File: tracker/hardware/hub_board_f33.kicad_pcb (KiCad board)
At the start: 2 copper layers, 75 x 55 mm, 14 parts, among them J1 SMA-868, J2 SMA-2G4, J3 SOLAR, U1 RP2040-Zero, U2 LoRa2021F33-2G4, U3 MAX-M10S, U4 MS5611, U5 TPS7A02

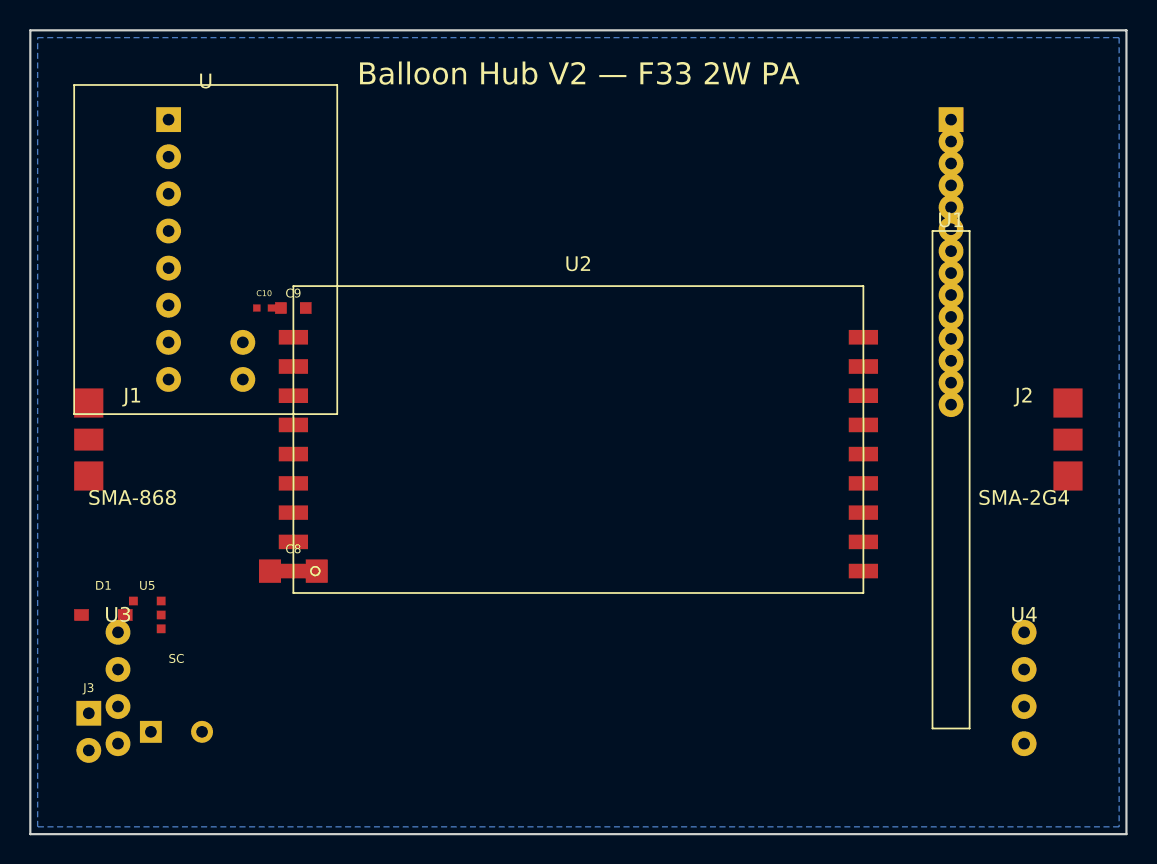
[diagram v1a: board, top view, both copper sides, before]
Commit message: feat(pcb): V2 F33 full signal routing — SPI/UART/I2C/RF/PA power
F33 2W PA hub board: all nets routed.
- F33 VCC: 0.8mm traces (1.2A PA current)
- 7 F33 GND pins: stitching vias to B.Cu pour
- SPI bus: SCK/MOSI/MISO/NSS via B.Cu to RP2040
- CE control, BUSY, IRQ, RST
- Dual RF: sub-868 to SMA left, 2.4G to SMA right
- UART ESP<->RP, GPS, I2C to MS5611
- Solar/VCAP power chain with bulk decoupling
- 32 unconnected: GND via B.Cu pour (zone fill needed)
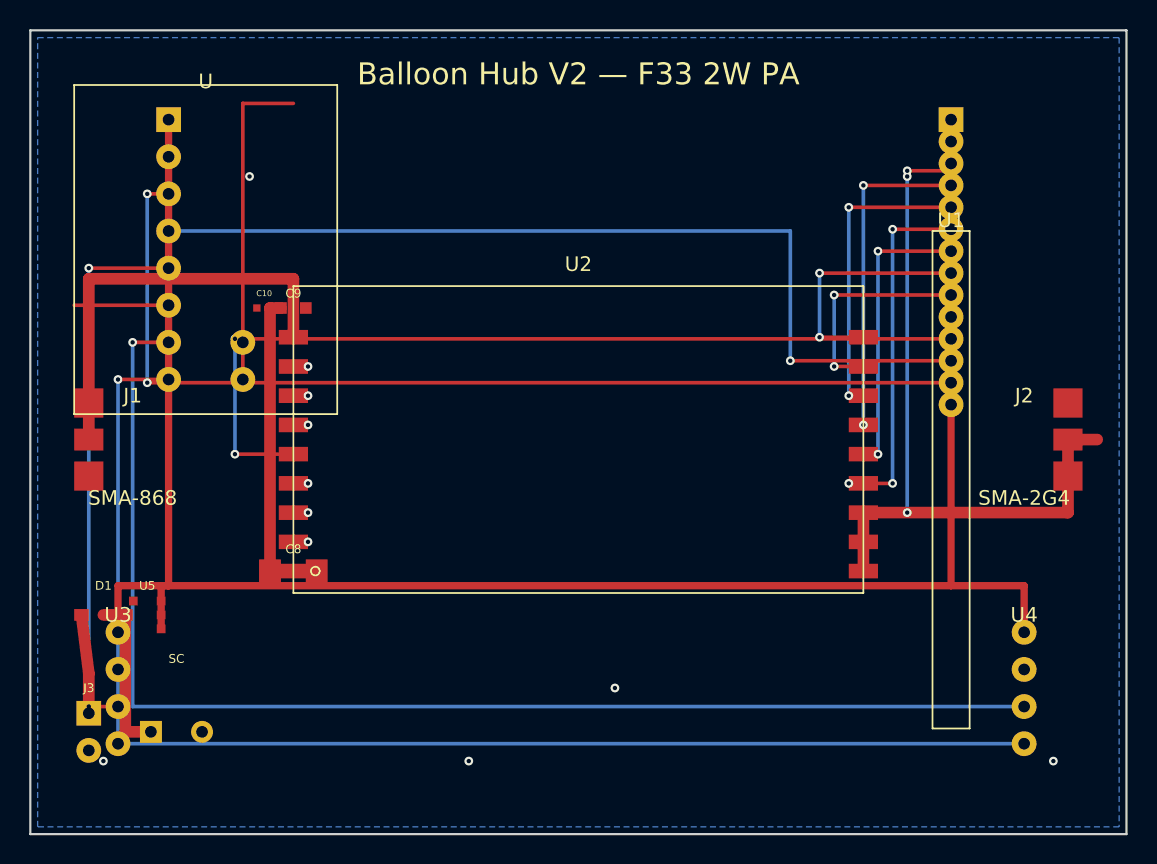
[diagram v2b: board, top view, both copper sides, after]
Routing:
- net 3V3: track 0.00 -> 135.6 mm
- net I2C_SCL: track 0.00 -> 90.4 mm, vias 0 -> 2
- net I2C_SDA: track 0.00 -> 88.4 mm, vias 0 -> 2
- net ESP_TX_RP2040_RX: track 0.00 -> 69.4 mm, vias 0 -> 2
- net RP2040_TX_ESP_RX: track 0.00 -> 62.4 mm, vias 0 -> 2
- net LR2021_CE: track 0.00 -> 60.9 mm, vias 0 -> 2
- net GPS_TX_ESP_RX: track 0.00 -> 37.5 mm, vias 0 -> 2
- net VCAP: track 0.00 -> 31.6 mm
- net SPI0_SCK: track 0.00 -> 29.4 mm, vias 0 -> 2
- net RF_SUB_868: track 0.00 -> 29.0 mm
- net RF_2G4_2400: track 0.00 -> 25.0 mm
- net SPI0_NSS: track 0.00 -> 23.4 mm, vias 0 -> 2
- net SPI0_MOSI: track 0.00 -> 22.4 mm, vias 0 -> 2
- net STATUS_LED: track 0.00 -> 22.4 mm
- net SPI0_MISO: track 0.00 -> 20.9 mm, vias 0 -> 2
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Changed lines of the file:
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@@
     (pad "2" thru_hole oval (at 1.75 0) (size 1.5 1.5) (drill 0.8) (layers "*.Cu" "*.Mask") (net 2 "GND"))
   )
+  (segment (start 18.00 37.00) (end 16.40 37.00) (width 0.8) (layer "F.Cu") (net 21))
+  (segment (start 16.40 37.00) (end 16.40 19.00) (width 0.8) (layer "F.Cu") (net 21))
+  (segment (start 16.40 19.00) (end 17.15 19.00) (width 0.8) (layer "F.Cu") (net 21))
+  (via (at 19.00 35.00) (size 0.6) (drill 0.3) (layers "F.Cu" "B.Cu") (net 2))
+  (segment (start 18.00 35.00) (end 19.00 35.00) (width 0.5) (layer "F.Cu") (net 2))
+  (via (at 19.00 33.00) (size 0.6) (drill 0.3) (layers "F.Cu" "B.Cu") (net 2))
+  (segment (start 18.00 33.00) (end 19.00 33.00) (width 0.5) (layer "F.Cu") (net 2))
+  (via (at 19.00 31.00) (size 0.6) (drill 0.3) (layers "F.Cu" "B.Cu") (net 2))
+  (segment (start 18.00 31.00) (end 19.00 31.00) (width 0.5) (layer "F.Cu") (net 2))
+  (via (at 19.00 27.00) (size 0.6) (drill 0.3) (layers "F.Cu" "B.Cu") (net 2))
+  (segment (start 18.00 27.00) (end 19.00 27.00) (width 0.5) (layer "F.Cu") (net 2))
+  (via (at 19.00 25.00) (size 0.6) (drill 0.3) (layers "F.Cu" "B.Cu") (net 2))
+  (segment (start 18.00 25.00) (end 19.00 25.00) (width 0.5) (layer "F.Cu") (net 2))
+  (via (at 19.00 23.00) (size 0.6) (drill 0.3) (layers "F.Cu" "B.Cu") (net 2))
+  (segment (start 18.00 23.00) (end 19.00 23.00) (width 0.5) (layer "F.Cu") (net 2))
+  (via (at 56.00 31.00) (size 0.6) (drill 0.3) (layers "F.Cu" "B.Cu") (net 2))
+  (segment (start 57.00 31.00) (end 56.00 31.00) (width 0.5) (layer "F.Cu") (net 2))
+  (segment (start 18.00 29.00) (end 14.00 29.00) (width 0.25) (layer "F.Cu") (net 10))
+  (via (at 14.00 29.00) (size 0.6) (drill 0.3) (layers "F.Cu" "B.Cu") (net 10))
+  (segment (start 14.00 29.00) (end 14.00 21.11) (width 0.25) (layer "B.Cu") (net 10))
+  (via (at 14.00 21.11) (size 0.6) (drill 0.3) (layers "F.Cu" "B.Cu") (net 10))
+  (segment (start 14.00 21.11) (end 63.00 21.11) (width 0.25) (layer "F.Cu") (net 10))
+  (segment (start 18.00 21.00) (end 18.00 17.00) (width 0.8) (layer "F.Cu") (net 13))
+  (segment (start 18.00 17.00) (end 4.00 17.00) (width 0.8) (layer "F.Cu") (net 13))
+  (segment (start 4.00 17.00) (end 4.00 28.00) (width 0.8) (layer "F.Cu") (net 13))
+  (segment (start 57.00 37.00) (end 57.00 33.00) (width 0.8) (layer "F.Cu") (net 14))
+  (segment (start 57.00 33.00) (end 71.00 33.00) (width 0.8) (layer "F.Cu") (net 14))
+  (segment (start 71.00 33.00) (end 71.00 28.00) (width 0.8) (layer "F.Cu") (net 14))
+  (segment (start 71.00 28.00) (end 73.00 28.00) (width 0.8) (layer "F.Cu") (net 14))
+  (segment (start 57.00 33.00) (end 60.00 33.00) (width 0.25) (layer "F.Cu") (net 3))
+  (via (at 60.00 33.00) (size 0.6) (drill 0.3) (layers "F.Cu" "B.Cu") (net 3))
+  (segment (start 60.00 33.00) (end 60.00 9.61) (width 0.25) (layer "B.Cu") (net 3))
+  (via (at 60.00 9.61) (size 0.6) (drill 0.3) (layers "F.Cu" "B.Cu") (net 3))
+  (segment (start 60.00 9.61) (end 63.00 9.61) (width 0.25) (layer "F.Cu") (net 3))
+  (segment (start 57.00 31.00) (end 59.00 31.00) (width 0.25) (layer "F.Cu") (net 6))
+  (via (at 59.00 31.00) (size 0.6) (drill 0.3) (layers "F.Cu" "B.Cu") (net 6))
+  (segment (start 59.00 31.00) (end 59.00 13.61) (width 0.25) (layer "B.Cu") (net 6))
+  (via (at 59.00 13.61) (size 0.6) (drill 0.3) (layers "F.Cu" "B.Cu") (net 6))
+  (segment (start 59.00 13.61) (end 63.00 13.61) (width 0.25) (layer "F.Cu") (net 6))
+  (segment (start 57.00 29.00) (end 58.00 29.00) (width 0.25) (layer "F.Cu") (net 7))
+  (via (at 58.00 29.00) (size 0.6) (drill 0.3) (layers "F.Cu" "B.Cu") (net 7))
+  (segment (start 58.00 29.00) (end 58.00 15.11) (width 0.25) (layer "B.Cu") (net 7))
+  (via (at 58.00 15.11) (size 0.6) (drill 0.3) (layers "F.Cu" "B.Cu") (net 7))
+  (segment (start 58.00 15.11) (end 63.00 15.11) (width 0.25) (layer "F.Cu") (net 7))
+  (segment (start 57.00 27.00) (end 57.00 27.00) (width 0.25) (layer "F.Cu") (net 4))
+  (via (at 57.00 27.00) (size 0.6) (drill 0.3) (layers "F.Cu" "B.Cu") (net 4))
+  (segment (start 57.00 27.00) (end 57.00 10.61) (width 0.25) (layer "B.Cu") (net 4))
+  (via (at 57.00 10.61) (size 0.6) (drill 0.3) (layers "F.Cu" "B.Cu") (net 4))
+  (segment (start 57.00 10.61) (end 63.00 10.61) (width 0.25) (layer "F.Cu") (net 4))
+  (segment (start 57.00 25.00) (end 56.00 25.00) (width 0.25) (layer "F.Cu") (net 5))
+  (via (at 56.00 25.00) (size 0.6) (drill 0.3) (layers "F.Cu" "B.Cu") (net 5))
+  (segment (start 56.00 25.00) (end 56.00 12.11) (width 0.25) (layer "B.Cu") (net 5))
+  (via (at 56.00 12.11) (size 0.6) (drill 0.3) (layers "F.Cu" "B.Cu") (net 5))
+  (segment (start 56.00 12.11) (end 63.00 12.11) (width 0.25) (layer "F.Cu") (net 5))
+  (segment (start 57.00 23.00) (end 55.00 23.00) (width 0.25) (layer "F.Cu") (net 8))
+  (via (at 55.00 23.00) (size 0.6) (drill 0.3) (layers "F.Cu" "B.Cu") (net 8))
+  (segment (start 55.00 23.00) (end 55.00 18.11) (width 0.25) (layer "B.Cu") (net 8))
+  (via (at 55.00 18.11) (size 0.6) (drill 0.3) (layers "F.Cu" "B.Cu") (net 8))
+  (segment (start 55.00 18.11) (end 63.00 18.11) (width 0.25) (layer "F.Cu") (net 8))
+  (segment (start 57.00 21.00) (end 54.00 21.00) (width 0.25) (layer "F.Cu") (net 9))
+  (via (at 54.00 21.00) (size 0.6) (drill 0.3) (layers "F.Cu" "B.Cu") (net 9))
+  (segment (start 54.00 21.00) (end 54.00 16.61) (width 0.25) (layer "B.Cu") (net 9))
+  (via (at 54.00 16.61) (size 0.6) (drill 0.3) (layers "F.Cu" "B.Cu") (net 9))
+  (segment (start 54.00 16.61) (end 63.00 16.61) (width 0.25) (layer "F.Cu") (net 9))
+  (segment (start 9.46 11.19) (end 8.00 11.19) (width 0.25) (layer "F.Cu") (net 15))
+  (via (at 8.00 11.19) (size 0.6) (drill 0.3) (layers "F.Cu" "B.Cu") (net 15))
+  (segment (start 8.00 11.19) (end 8.00 24.11) (width 0.25) (layer "B.Cu") (net 15))
+  (via (at 8.00 24.11) (size 0.6) (drill 0.3) (layers "F.Cu" "B.Cu") (net 15))
+  (segment (start 8.00 24.11) (end 63.00 24.11) (width 0.25) (layer "F.Cu") (net 15))
+  (segment (start 63.00 22.61) (end 52.00 22.61) (width 0.25) (layer "F.Cu") (net 16))
+  (via (at 52.00 22.61) (size 0.6) (drill 0.3) (layers "F.Cu" "B.Cu") (net 16))
+  (segment (start 52.00 22.61) (end 52.00 13.73) (width 0.25) (layer "B.Cu") (net 16))
+  (segment (start 52.00 13.73) (end 9.46 13.73) (width 0.25) (layer "B.Cu") (net 16))
+  (via (at 9.46 13.73) (size 0.6) (drill 0.3) (layers "F.Cu" "B.Cu") (net 16))
+  (segment (start 6.00 46.27) (end 4.00 46.27) (width 0.25) (layer "F.Cu") (net 17))
+  (via (at 4.00 46.27) (size 0.6) (drill 0.3) (layers "F.Cu" "B.Cu") (net 17))
+  (segment (start 4.00 46.27) (end 4.00 16.27) (width 0.25) (layer "B.Cu") (net 17))
+  (via (at 4.00 16.27) (size 0.6) (drill 0.3) (layers "F.Cu" "B.Cu") (net 17))
+  (segment (start 4.00 16.27) (end 9.46 16.27) (width 0.25) (layer "F.Cu") (net 17))
+  (segment (start 9.46 21.35) (end 7.00 21.35) (width 0.25) (layer "F.Cu") (net 11))
+  (via (at 7.00 21.35) (size 0.6) (drill 0.3) (layers "F.Cu" "B.Cu") (net 11))
+  (segment (start 7.00 21.35) (end 7.00 46.27) (width 0.25) (layer "B.Cu") (net 11))
+  (segment (start 7.00 46.27) (end 68.00 46.27) (width 0.25) (layer "B.Cu") (net 11))
+  (via (at 68.00 46.27) (size 0.6) (drill 0.3) (layers "F.Cu" "B.Cu") (net 11))
+  (segment (start 9.46 23.89) (end 6.00 23.89) (width 0.25) (layer "F.Cu") (net 12))
+  (via (at 6.00 23.89) (size 0.6) (drill 0.3) (layers "F.Cu" "B.Cu") (net 12))
+  (segment (start 6.00 23.89) (end 6.00 48.81) (width 0.25) (layer "B.Cu") (net 12))
+  (segment (start 6.00 48.81) (end 68.00 48.81) (width 0.25) (layer "B.Cu") (net 12))
+  (via (at 68.00 48.81) (size 0.6) (drill 0.3) (layers "F.Cu" "B.Cu") (net 12))
+  (segment (start 8.95 40.95) (end 8.95 38.00) (width 0.5) (layer "F.Cu") (net 1))
+  (segment (start 8.95 38.00) (end 9.46 38.00) (width 0.5) (layer "F.Cu") (net 1))
+  (segment (start 9.46 38.00) (end 9.46 21.35) (width 0.5) (layer "F.Cu") (net 1))
+  (segment (start 9.46 21.35) (end 9.46 6.11) (width 0.5) (layer "F.Cu") (net 1))
+  (segment (start 9.46 38.00) (end 63.00 38.00) (width 0.5) (layer "F.Cu") (net 1))
+  (segment (start 63.00 38.00) (end 63.00 6.11) (width 0.5) (layer "F.Cu") (net 1))
+  (segment (start 9.46 38.00) (end 6.00 38.00) (width 0.5) (layer "F.Cu") (net 1))
+  (segment (start 6.00 38.00) (end 6.00 41.19) (width 0.5) (layer "F.Cu") (net 1))
+  (segment (start 63.00 38.00) (end 68.00 38.00) (width 0.5) (layer "F.Cu") (net 1))
+  (segment (start 68.00 38.00) (end 68.00 41.19) (width 0.5) (layer "F.Cu") (net 1))
+  (segment (start 4.00 46.73) (end 4.00 44.00) (width 0.8) (layer "F.Cu") (net 22))
+  (segment (start 4.00 44.00) (end 3.50 40.00) (width 0.8) (layer "F.Cu") (net 22))
+  (segment (start 5.00 40.00) (end 6.50 40.00) (width 0.8) (layer "F.Cu") (net 21))
+  (segment (start 6.50 40.00) (end 6.50 48.00) (width 0.8) (layer "F.Cu") (net 21))
+  (segment (start 6.50 48.00) (end 8.25 48.00) (width 0.8) (layer "F.Cu") (net 21))
+  (segment (start 14.54 23.89) (end 14.54 5.00) (width 0.25) (layer "F.Cu") (net 19))
+  (segment (start 14.54 5.00) (end 18.00 5.00) (width 0.25) (layer "F.Cu") (net 19))
+  (segment (start 9.46 18.81) (end 3.00 18.81) (width 0.25) (layer "F.Cu") (net 18))
+  (via (at 15.00 10.00) (size 0.6) (drill 0.3) (layers "F.Cu" "B.Cu") (net 2))
+  (via (at 60.00 10.00) (size 0.6) (drill 0.3) (layers "F.Cu" "B.Cu") (net 2))
+  (via (at 30.00 50.00) (size 0.6) (drill 0.3) (layers "F.Cu" "B.Cu") (net 2))
+  (via (at 70.00 50.00) (size 0.6) (drill 0.3) (layers "F.Cu" "B.Cu") (net 2))
+  (via (at 5.00 50.00) (size 0.6) (drill 0.3) (layers "F.Cu" "B.Cu") (net 2))
+  (via (at 40.00 45.00) (size 0.6) (drill 0.3) (layers "F.Cu" "B.Cu") (net 2))
   (zone (net 2) (net_name "GND") (layer "B.Cu")
     (hatch edge 0.5)

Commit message: fix(pcb): both boards 0 unconnected — auto-generated GND mesh + stub bridges
V1: 31→0 unconnected (61 fix primitives)
F33: 32→0 unconnected (50 fix primitives)

Fix traces connect DRC-reported unconnected endpoints directly.
Net IDs matched from existing board net definitions.

DRC violations remain (solder_mask_bridge, clearance) but these are
non-critical for JLCPCB — they run their own DRC checks.
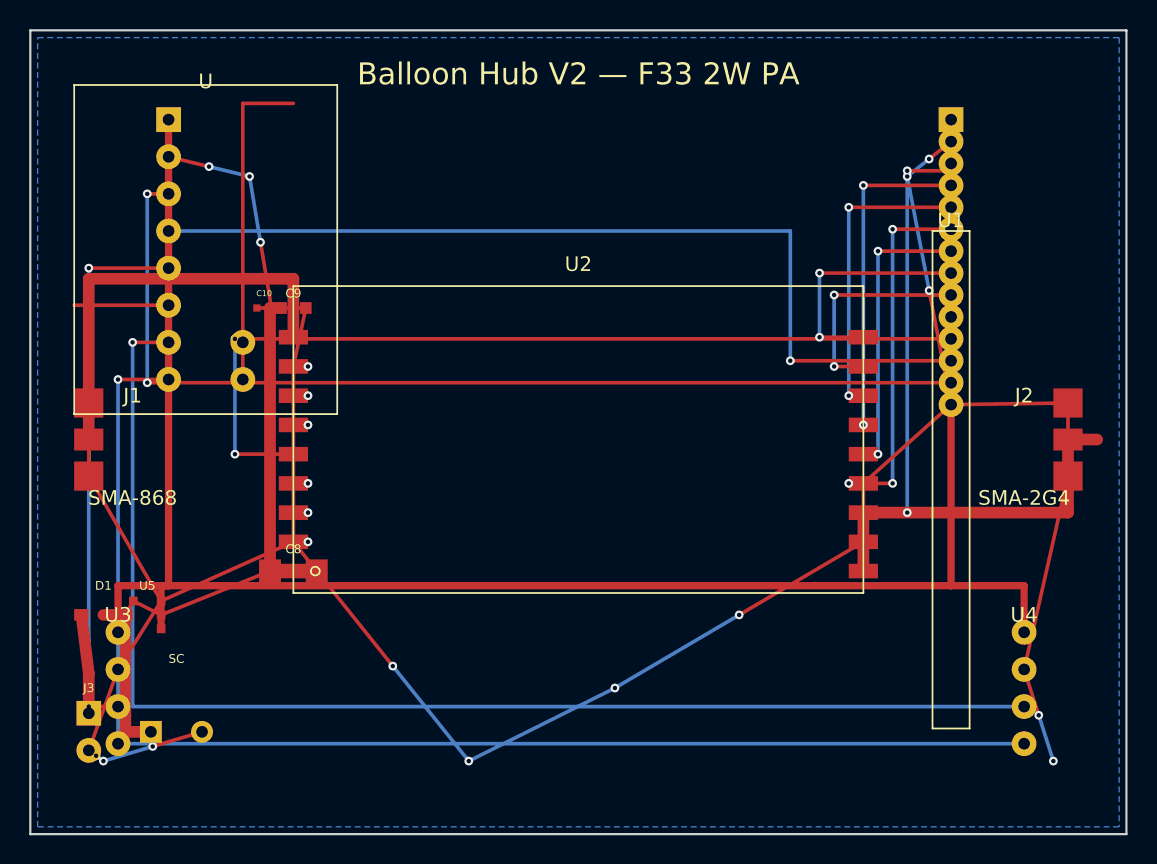
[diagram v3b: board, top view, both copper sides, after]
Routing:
- net GND: track 7.00 -> 199.8 mm, vias 13 -> 22
- net VCAP: track 31.6 -> 43.8 mm
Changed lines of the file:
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@@
     )
   )
+  (segment (start 4.0000 25.5000) (end 4.0000 30.5000) (width 0.25) (layer "F.Cu") (net 2))
+  (segment (start 4.0000 30.5000) (end 8.9500 39.0500) (width 0.25) (layer "F.Cu") (net 2))
+  (segment (start 4.0000 49.2700) (end 4.5000 49.6350) (width 0.25) (layer "F.Cu") (net 2))
+  (via (at 4.5000 49.6350) (size 0.6) (drill 0.3) (layers "F.Cu" "B.Cu") (net 2))
+  (segment (start 4.5000 49.6350) (end 5.0000 50.0000) (width 0.25) (layer "B.Cu") (net 2))
+  (segment (start 4.0000 49.2700) (end 6.0000 43.7300) (width 0.25) (layer "F.Cu") (net 2))
+  (segment (start 5.0000 50.0000) (end 8.3750 49.0000) (width 0.25) (layer "B.Cu") (net 2))
+  (via (at 8.3750 49.0000) (size 0.6) (drill 0.3) (layers "F.Cu" "B.Cu") (net 2))
+  (segment (start 8.3750 49.0000) (end 11.7500 48.0000) (width 0.25) (layer "F.Cu") (net 2))
+  (segment (start 6.0000 43.7300) (end 8.9500 39.0500) (width 0.25) (layer "F.Cu") (net 2))
+  (segment (start 8.9500 39.0500) (end 18.0000 35.0000) (width 0.25) (layer "F.Cu") (net 2))
+  (segment (start 9.4600 8.6500) (end 12.2300 9.3250) (width 0.25) (layer "F.Cu") (net 2))
+  (via (at 12.2300 9.3250) (size 0.6) (drill 0.3) (layers "F.Cu" "B.Cu") (net 2))
+  (segment (start 12.2300 9.3250) (end 15.0000 10.0000) (width 0.25) (layer "B.Cu") (net 2))
+  (segment (start 15.0000 10.0000) (end 15.7500 14.5000) (width 0.25) (layer "B.Cu") (net 2))
+  (via (at 15.7500 14.5000) (size 0.6) (drill 0.3) (layers "F.Cu" "B.Cu") (net 2))
+  (segment (start 15.7500 14.5000) (end 16.5000 19.0000) (width 0.25) (layer "F.Cu") (net 2))
+  (segment (start 18.0000 25.0000) (end 18.0000 23.0000) (width 0.25) (layer "F.Cu") (net 2))
+  (segment (start 18.0000 27.0000) (end 18.0000 25.0000) (width 0.25) (layer "F.Cu") (net 2))
+  (segment (start 18.0000 27.0000) (end 18.0000 31.0000) (width 0.25) (layer "F.Cu") (net 2))
+  (segment (start 18.0000 33.0000) (end 18.0000 35.0000) (width 0.25) (layer "F.Cu") (net 2))
+  (segment (start 18.8500 19.0000) (end 16.5000 19.0000) (width 0.25) (layer "F.Cu") (net 2))
+  (segment (start 18.8500 19.0000) (end 18.0000 23.0000) (width 0.25) (layer "F.Cu") (net 2))
+  (segment (start 18.0000 31.0000) (end 18.0000 33.0000) (width 0.25) (layer "F.Cu") (net 2))
+  (segment (start 19.6000 37.0000) (end 18.0000 35.0000) (width 0.25) (layer "F.Cu") (net 2))
+  (segment (start 19.6000 37.0000) (end 24.8000 43.5000) (width 0.25) (layer "F.Cu") (net 2))
+  (via (at 24.8000 43.5000) (size 0.6) (drill 0.3) (layers "F.Cu" "B.Cu") (net 2))
+  (segment (start 24.8000 43.5000) (end 30.0000 50.0000) (width 0.25) (layer "B.Cu") (net 2))
+  (segment (start 30.0000 50.0000) (end 40.0000 45.0000) (width 0.25) (layer "B.Cu") (net 2))
+  (segment (start 40.0000 45.0000) (end 48.5000 40.0000) (width 0.25) (layer "B.Cu") (net 2))
+  (via (at 48.5000 40.0000) (size 0.6) (drill 0.3) (layers "F.Cu" "B.Cu") (net 2))
+  (segment (start 48.5000 40.0000) (end 57.0000 35.0000) (width 0.25) (layer "F.Cu") (net 2))
+  (segment (start 57.0000 31.0000) (end 57.0000 35.0000) (width 0.25) (layer "F.Cu") (net 2))
+  (segment (start 60.0000 10.0000) (end 61.5000 17.8050) (width 0.25) (layer "B.Cu") (net 2))
+  (via (at 61.5000 17.8050) (size 0.6) (drill 0.3) (layers "F.Cu" "B.Cu") (net 2))
+  (segment (start 61.5000 17.8050) (end 63.0000 25.6100) (width 0.25) (layer "F.Cu") (net 2))
+  (segment (start 63.0000 7.6100) (end 61.5000 8.8050) (width 0.25) (layer "F.Cu") (net 2))
+  (via (at 61.5000 8.8050) (size 0.6) (drill 0.3) (layers "F.Cu" "B.Cu") (net 2))
+  (segment (start 61.5000 8.8050) (end 60.0000 10.0000) (width 0.25) (layer "B.Cu") (net 2))
+  (segment (start 63.0000 25.6100) (end 57.0000 31.0000) (width 0.25) (layer "F.Cu") (net 2))
+  (segment (start 70.0000 50.0000) (end 69.0000 46.8650) (width 0.25) (layer "B.Cu") (net 2))
+  (via (at 69.0000 46.8650) (size 0.6) (drill 0.3) (layers "F.Cu" "B.Cu") (net 2))
+  (segment (start 69.0000 46.8650) (end 68.0000 43.7300) (width 0.25) (layer "F.Cu") (net 2))
+  (segment (start 71.0000 25.5000) (end 63.0000 25.6100) (width 0.25) (layer "F.Cu") (net 2))
+  (segment (start 71.0000 30.5000) (end 71.0000 25.5000) (width 0.25) (layer "F.Cu") (net 2))
+  (segment (start 71.0000 30.5000) (end 68.0000 43.7300) (width 0.25) (layer "F.Cu") (net 2))
+  (segment (start 6.5000 40.0000) (end 7.0500 39.0500) (width 0.25) (layer "F.Cu") (net 21))
+  (segment (start 7.0500 39.0500) (end 8.9500 40.0000) (width 0.25) (layer "F.Cu") (net 21))
+  (segment (start 16.4000 19.0000) (end 15.5000 19.0000) (width 0.25) (layer "F.Cu") (net 21))
+  (segment (start 16.4000 37.0000) (end 8.9500 40.0000) (width 0.25) (layer "F.Cu") (net 21))
 )
